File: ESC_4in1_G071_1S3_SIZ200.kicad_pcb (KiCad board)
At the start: 4 copper layers, 28 x 28 mm, 185 parts, among them J1 Conn_01x10, U1 STM32G071GBU6, U10 NCP81161MNTBG, U11 SIZ200DT-T1-GE3, U12 NCP81161MNTBG, U13 SIZ200DT-T1-GE3, U14 TPS630701, U15 TPS72733DSE, U16 INA186A2, U17 STM32G071GBU6, U18 NCP81161MNTBG, U19 SIZ200DT-T1-GE3, U2 NCP81161MNTBG, U20 NCP81161MNTBG, U21 STM32G071GBU6, U22 SIZ200DT-T1-GE3, U23 NCP81161MNTBG, U24 SIZ200DT-T1-GE3, U25 NCP81161MNTBG, U26 SIZ200DT-T1-GE3, U27 NCP81161MNTBG, U28 STM32G071GBU6, U29 SIZ200DT-T1-GE3, U3 SIZ200DT-T1-GE3, U30 NCP81161MNTBG, U31 SIZ200DT-T1-GE3, U4 NCP81161MNTBG, U5 SIZ200DT-T1-GE3, U6 NCP81161MNTBG, U7 SIZ200DT-T1-GE3, U8 NCP81161MNTBG, U9 SIZ200DT-T1-GE3

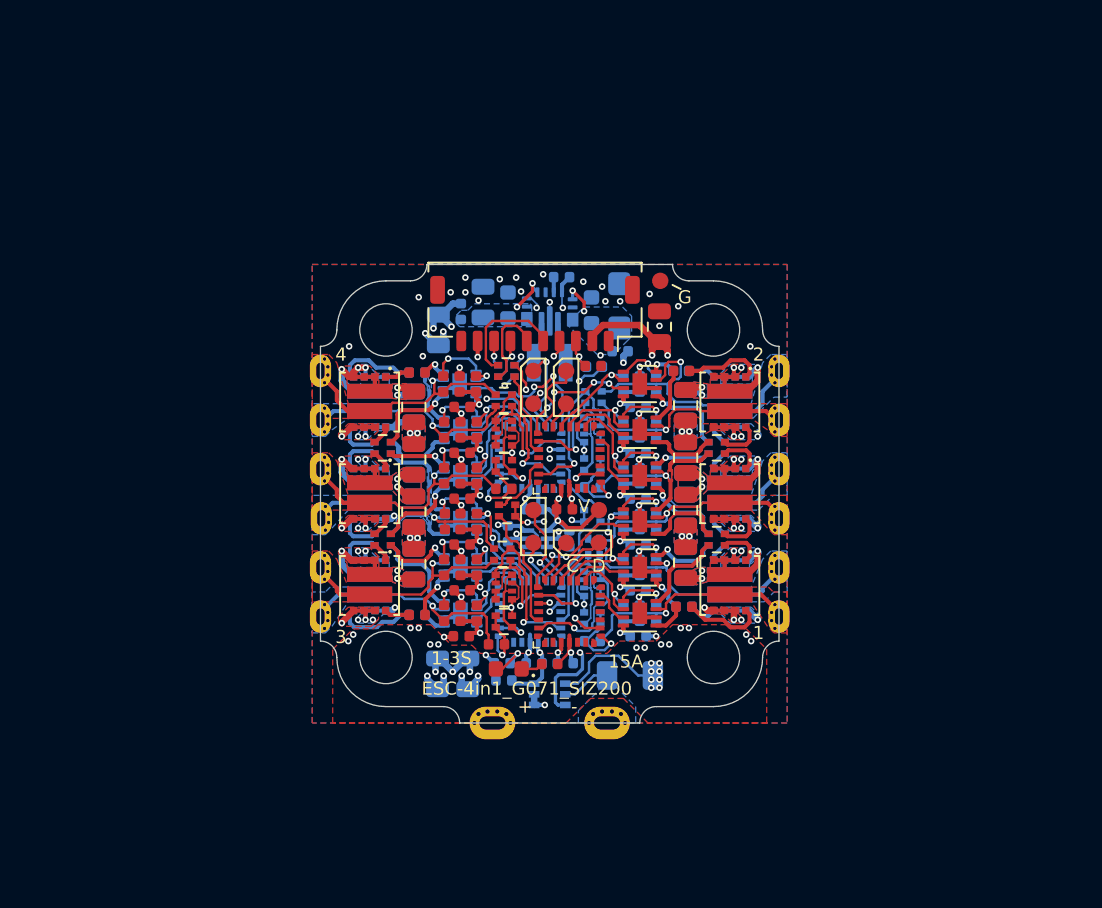
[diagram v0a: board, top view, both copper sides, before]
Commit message: general redesign 1 current sensor per ESC
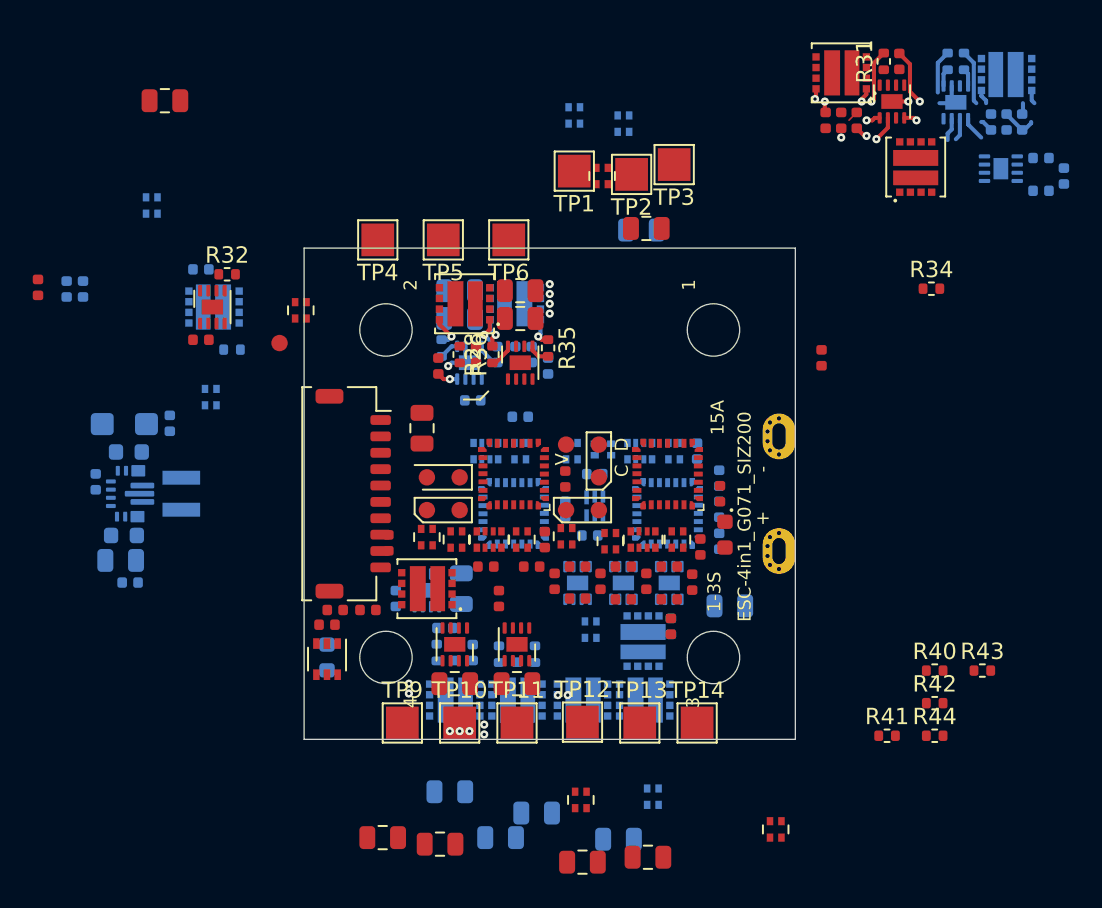
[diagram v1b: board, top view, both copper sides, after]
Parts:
- removed C57, C58, C59, C60, C61, C62, C64, C65, C66, C67, C68, C69: 10u, Capacitor_SMD:C_0402_1005Metric
- added R28: 10R0, Resistor_SMD:R_0402_1005Metric, F.Cu at (132.5, 66.5)
- added R29: 10R0, Resistor_SMD:R_0402_1005Metric, B.Cu at (129.4, 66.1)
- added R30: 10R0, Resistor_SMD:R_0402_1005Metric, B.Cu at (160.3, 48.6)
- added R31: 10R0, Resistor_SMD:R_0402_1005Metric, F.Cu at (156.4, 48.6)
- added R32: 10R0, Resistor_SMD:R_0402_1005Metric, F.Cu at (116.3, 61.6)
- added R33: 10R0, Resistor_SMD:R_0402_1005Metric, B.Cu at (161.3, 48.6)
- added R34: 10R0, Resistor_SMD:R_0402_1005Metric, F.Cu at (159.3, 62.5)
- added R35: 10R0, Resistor_SMD:R_0402_1005Metric, F.Cu at (135.9, 66.1)
- added R36: 10k, Resistor_SMD:R_0402_1005Metric, F.Cu at (130.5, 66.5)
- added R37: 10k, Resistor_SMD:R_0402_1005Metric, B.Cu at (116.6, 66.2)
- added R38: 10R0, Resistor_SMD:R_0402_1005Metric, B.Cu at (135.1, 84.8)
- added R39: 10R0, Resistor_SMD:R_0402_1005Metric, B.Cu at (129.1, 84.7)
- added R40: 10R0, Resistor_SMD:R_0402_1005Metric, F.Cu at (159.5, 85.8)
- added R41: 10R0, Resistor_SMD:R_0402_1005Metric, F.Cu at (156.6, 89.8)
- added R42: 10R0, Resistor_SMD:R_0402_1005Metric, F.Cu at (159.5, 87.8)
- added R43: 10R0, Resistor_SMD:R_0402_1005Metric, F.Cu at (162.4, 85.8)
- added R44: 10R0, Resistor_SMD:R_0402_1005Metric, F.Cu at (159.5, 89.8)
- added R45: 10R0, Resistor_SMD:R_0402_1005Metric, B.Cu at (132.9, 84.8)
- C1, C10, C38, C51, C63, R19, R26, R3, U16, U20, U23: moved to F.Cu
- C11, C23, C28, C30, C33, C35, C5, C6: value 100n -> 1u
- C26: value 100n -> 1u; moved to B.Cu
- C27, C29, R23, R24, U10, U2, U24, U29, U6: moved to B.Cu
- C4, C7, C9: value 100n -> 1u; moved to F.Cu
- R1: footprint Resistor_SMD:R_1206_3216Metric -> 11_PSoC_FC_whoop:C_0603_1608Metric_dense
- TP1, TP10, TP11, TP12, TP13, TP14, TP2, TP3, TP4, TP5, TP6, TP9: footprint 11_PSoC_FC_whoop:esc_pad_relaxed_n4 -> 11_PSoC_FC_whoop:ESC_Pad_2.0x2.0mm
- moved C43 40.5 mm to (112.5, 51.0), turned to 180 degrees
- moved C6 38.3 mm to (167.4, 55.6), turned to 270 degrees
- moved C5 37.0 mm to (164.8, 52.3), turned to 270 degrees
- moved C3 36.4 mm to (166.0, 54.5), turned to 180 degrees
- moved R5 36.3 mm to (166.0, 56.5), turned to 180 degrees
- moved R4 35.9 mm to (163.9, 52.3), turned to 270 degrees
- moved R26 35.8 mm to (157.3, 48.6), turned to 270 degrees
- moved C11 35.6 mm to (106.5, 62.5), turned to 270 degrees
- moved U5 35.5 mm to (163.9, 49.4), turned to 90 degrees
- moved U6 35.0 mm to (163.6, 55.1)
- moved C20 34.2 mm to (104.8, 62.4), turned to 270 degrees
- moved C2 34.0 mm to (162.9, 52.3), turned to 270 degrees
- moved U4 32.4 mm to (156.9, 51.0), turned to 90 degrees
- moved U2 32.1 mm to (160.8, 51.1), turned to 90 degrees
- moved U9 32.0 mm to (115.5, 63.6), turned to 90 degrees
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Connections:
- C37 pad 2: +BATT -> VESC4
- C38 pad 2: +BATT -> VESC4
- C39 pad 2: +BATT -> VESC4
- R1 pad 1: GND -> +BATT
- R1 pad 2: /Batt- -> VESC4
- RN1 pad 1: /ESC1_A_DRVL -> Net-(RN1-Pad1)
- RN1 pad 2: /ESC1_C_DRVH -> Net-(RN1-Pad2)
- RN1 pad 3: /ESC1_C_GH -> Net-(RN1-Pad3)
- RN1 pad 4: /ESC1_A_GL -> Net-(RN1-Pad4)
- RN10 pad 1: /ESC2_A -> Net-(RN10-Pad1)
- RN10 pad 2: /ESC2_B -> Net-(RN10-Pad2)
- RN10 pad 3: /ESC2_MB -> Net-(RN10-Pad3)
- RN10 pad 4: /ESC2_MA -> Net-(RN10-Pad4)
- RN14 pad 1: /ESC4_C_DRVH -> Net-(RN14-Pad1)
- RN14 pad 2: /ESC4_A_DRVL -> Net-(RN14-Pad2)
- RN14 pad 3: /ESC4_A_GL -> Net-(RN14-Pad3)
- RN14 pad 4: /ESC4_C_GH -> Net-(RN14-Pad4)
- RN19 pad 1: /ESC3_A_DRVL -> Net-(RN19-Pad1)
- RN19 pad 2: /ESC3_C_DRVH -> Net-(RN19-Pad2)
- RN19 pad 3: /ESC3_C_GH -> Net-(RN19-Pad3)
- RN19 pad 4: /ESC3_A_GL -> Net-(RN19-Pad4)
- RN20 pad 1: /ESC3_B_DRVH -> Net-(RN20-Pad1)
- RN20 pad 2: /ESC4_C_DRVL -> Net-(RN20-Pad2)
- RN20 pad 3: /ESC4_C_GL -> Net-(RN20-Pad3)
- RN20 pad 4: /ESC3_B_GH -> Net-(RN20-Pad4)
- RN22 pad 1: /ESC4_B_DRVL -> Net-(RN22-Pad1)
- RN22 pad 2: /ESC3_A_DRVH -> Net-(RN22-Pad2)
- RN22 pad 3: /ESC3_A_GH -> Net-(RN22-Pad3)
- RN22 pad 4: /ESC4_B_GL -> Net-(RN22-Pad4)
- RN3 pad 1: /ESC1_B_DRVH -> Net-(RN3-Pad1)
- RN3 pad 2: /ESC2_C_DRVL -> Net-(RN3-Pad2)
- RN3 pad 3: /ESC2_C_GL -> Net-(RN3-Pad3)
- RN3 pad 4: /ESC1_B_GH -> Net-(RN3-Pad4)
- RN4 pad 1: /ESC2_C_DRVH -> Net-(RN4-Pad1)
- RN4 pad 2: /ESC2_A_DRVL -> Net-(RN4-Pad2)
- RN4 pad 3: /ESC2_A_GL -> Net-(RN4-Pad3)
- RN4 pad 4: /ESC2_C_GH -> Net-(RN4-Pad4)
- RN6 pad 1: /ESC2_B_DRVL -> Net-(RN6-Pad1)
- RN6 pad 2: /ESC1_A_DRVH -> Net-(RN6-Pad2)
- RN6 pad 3: /ESC1_A_GH -> Net-(RN6-Pad3)
- RN6 pad 4: /ESC2_B_GL -> Net-(RN6-Pad4)
- TP8 pad 1: /Batt- -> GND
- U16 pad 3: +3V3 -> +5V
- U16 pad 4: GND -> +BATT
- U16 pad 5: /Batt- -> VESC4
- U19 pad 2: +BATT -> VESC4
- U22 pad 2: +BATT -> VESC4
- U24 pad 2: +BATT -> VESC4
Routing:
- net GND: track 123.7 -> 6.98 mm, vias 94 -> 8
- net +BATT: track 88.6 -> 0.00 mm, vias 52 -> 4
- net +5V: track 41.7 -> 4.25 mm, vias 15 -> 2
- net Net-(R2-Pad2): track 25.4 -> 0.00 mm, vias 2 -> 0
- net +3V3: track 21.9 -> 0.00 mm, vias 5 -> 0
- net /ESCx_tele: track 18.1 -> 0.00 mm, vias 4 -> 0
- net /ESC3_IN: track 18.0 -> 0.00 mm, vias 2 -> 0
- net /ESC2_A: track 17.6 -> 0.00 mm, vias 1 -> 0
- net /ESC1_IN: track 16.9 -> 0.00 mm, vias 2 -> 0
- net /ESC1_B: track 15.7 -> 0.00 mm, vias 1 -> 0
- net /ESC2_C: track 14.5 -> 0.00 mm, vias 1 -> 0
- net /ESC4_C: track 14.2 -> 0.00 mm, vias 1 -> 0
- net /ESC1_C: track 14.0 -> 0.00 mm, vias 1 -> 0
- net /ESC2_B: track 14.0 -> 0.00 mm, vias 1 -> 0
- net /ESC4_A: track 13.9 -> 0.00 mm, vias 1 -> 0
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- removed copper zone on B.Cu, net +BATT
- removed copper zone on F.Cu, net +BATT
- removed copper zone on B.Cu, net /Batt-
- removed copper zone on F.Cu, net /ESC1_A
- removed copper zone on F.Cu, net /ESC1_A_DRVH
- removed copper zone on B.Cu, net /ESC1_B
- removed copper zone on F.Cu, net /ESC1_C
- removed copper zone on B.Cu, net /ESC2_A
- removed copper zone on F.Cu, net /ESC2_B
- removed copper zone on B.Cu, net /ESC2_C
- removed copper zone on B.Cu, net /ESC3_A
- removed copper zone on B.Cu, net /ESC3_A_DRVH
- removed copper zone on B.Cu, net /ESC3_A_DRVL
- removed copper zone on F.Cu, net /ESC3_B
- removed copper zone on B.Cu, net /ESC3_C
- removed copper zone on F.Cu, net /ESC4_A
- removed copper zone on B.Cu, net /ESC4_B
- removed copper zone on B.Cu, net /ESC4_B_DRVH
- removed copper zone on B.Cu, net /ESC4_B_DRVL
- removed copper zone on F.Cu, net /ESC4_C
- removed copper zone on B.Cu, net GND
- removed copper zone on F.Cu, net GND
- removed copper zone on B.Cu, net Net-(C13-Pad2)
- removed copper zone on B.Cu, net Net-(C15-Pad2)
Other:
- board size 28 x 28 mm -> 30 x 30 mm
- copper layers 4 -> 6
- net class Default: trace_width 0.25 -> 0.15; via_dia 0.8 -> 0.5; via_drill 0.4 -> 0.2
- rule via_min_size: 0.4 -> 0.5
- board text removed: "G"

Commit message: layout work
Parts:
- C24, C35, R42, U19: moved to B.Cu
- C37, U18, U21: moved to F.Cu
- moved R42 26.6 mm to (133.1, 84.3), turned to 90 degrees
- moved C45 19.4 mm to (135.2, 76.7), turned to 270 degrees
- moved R45 12.0 mm to (121.6, 80.7)
- moved C29 12.0 mm to (122.7, 80.7)
- moved R38 12.0 mm to (123.8, 80.7)
- moved R11 10.9 mm to (133.8, 81.9), turned to 0 degrees
- moved C24 9.56 mm to (134.2, 84.3), turned to 90 degrees
- moved U24 9.41 mm to (127.5, 80.8)
- moved R24 9.17 mm to (135.3, 84.3), turned to 90 degrees
- moved U19 8.81 mm to (134.1, 87.6), turned to 270 degrees
- moved TP11 7.00 mm to (127.0, 89.0)
- moved TP9 7.00 mm to (134.0, 89.0)
- moved U18 6.35 mm to (134.1, 83.9), turned to 270 degrees
- moved U23 4.53 mm to (130.6, 81.2), turned to 180 degrees
- moved C37 3.20 mm to (127.5, 81.6), turned to 0 degrees
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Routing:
- net VESC4: vias 0 -> 2
- net GND: vias 8 -> 11
- net /ESC3_A: vias 1 -> 0
- net +BATT: vias 4 -> 0
